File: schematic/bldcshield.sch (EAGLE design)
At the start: 51 parts, among them IC3 IR2101SMD, IC4 IR2101SMD, IC5 IR2101SMD, Q1 MOSFET-NCHANNELPTH2, Q2 MOSFET-NCHANNELPTH2, Q3 MOSFET-NCHANNELPTH2, Q4 MOSFET-NCHANNELPTH2, Q5 MOSFET-NCHANNELPTH2, Q6 MOSFET-NCHANNELPTH2, X1 MKDSN1,5/3-5,08, X2 MKDSN1,5/2-5,08

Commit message: redoing brf layout from scatch
deleted gerbers and backed up brd file
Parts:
- removed C20: 100pF, SmartPrj:C-EUC1206
- removed IC5: IR2101SMD, IR:IR2101SMD
- removed R29: 15k, SmartPrj:R-EU_R1206
- removed U$5: ARDUINO-NOHOLE, adafruit:ARDUINO-NOHOLE
- added C3: 100pF, SmartPrj:C-EUC1206
- added IC2: IR2101SMD, IR:IR2101SMD
- added Q7: MOSFET-NCHANNELPTH2, SparkFun:MOSFET-NCHANNELPTH2
- added R1: 200K, SmartPrj:R-EU_R1206
- Q3: value MOSFET-NCHANNELPTH2 -> Shield; device SparkFun:MOSFET-NCHANNELPTH2 -> adafruit:ARDUINOR3-NOIOREF-NOTEXT
- R10: value 10k -> 22k
- R11, R14, R6: value 10k -> 22
- R12, R13: value 22 -> 10k
- R15, R7: value 10k -> 100k
- R16, R8: value 22 -> 15k
- R17, R9: value 22 -> 22k
- R18: value 200K -> 22k
- R19: value 68k -> 22
- R2: value 22k -> 68k
- R20: value 100k -> 10k
- R21: value 15k -> 10k
- R22, R3: value 22k -> 22
- R23: value 22k -> 100k
- R24: value 100k -> 15k
- R25: value 15k -> 22k
- R27: value 22k -> 4.7k
- R28: value 100k -> 0.001; device SmartPrj:R-EU_R1206 -> resistor:R-US_R2512
- R4: value 4.7k -> 10k
- R5: value 0.001 -> 10k; device resistor:R-US_R2512 -> SmartPrj:R-EU_R1206
- X1: value MKDSN1,5/3-5,08 -> MKDSN1,5/2-5,08; device con-phoenix-508:MKDSN1,5/3-5,08 -> con-phoenix-508:MKDSN1,5/2-5,08
- X2: value MKDSN1,5/2-5,08 -> MKDSN1,5/3-5,08; device con-phoenix-508:MKDSN1,5/2-5,08 -> con-phoenix-508:MKDSN1,5/3-5,08
- renumbered C15 to C8, C16 to C5, C17 to C4, C18 to C1, C19 to C2, C21 to C7, D4 to D2, D5 to D1, IC4 to IC1
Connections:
- removed net N$20: C2.1, C20.1, C6.1, C7.1, IC1.COM, IC3.COM, IC5.COM, R10.1, R11.1, R14.1, R15.1, R19.1, R23.1, R27.1, R3.1, R5.1, R6.1, R7.1, X2-2.KL
- new net +3V3: Q3.3V
- net +5V: now also IC2.VCC, Q3.5V, Q3.VIN; no longer IC5.VCC, U$5.5V
- net BLDC1: now also C3.2, R7.2, R9.2, X2-1.KL; no longer C6.2, R2.2, R20.2, X1-1.KL
- net BLDC2: now also C6.2, IC2.VS, Q4.S, Q5.D, R15.2, R17.2, X2-2.KL; no longer C20.2, IC3.VS, Q3.S, Q4.D, R22.2, R24.2, X1-2.KL
- net BLDC3: now also IC3.VS, Q6.S, Q7.D, R23.2, R25.2, X2-3.KL; no longer IC5.VS, Q5.S, Q6.D, R26.2, R28.2, X1-3.KL
- net CURRENT: now also Q3.A0, Q5.S, Q7.S, R27.2, R28.2; no longer Q4.S, Q6.S, R4.2, R5.2, U$5.A0
- net EMF1: now also Q3.A3, R8.1; no longer R21.1, U$5.A3
- net EMF2: now also Q3.A2, R16.1; no longer R25.1, U$5.A2
- net EMF3: now also Q3.A1, R24.1; no longer R29.1, U$5.A1
- net GND: now also C2.1, C3.1, C6.1, C7.1, IC1.COM, IC2.COM, IC3.COM, Q3.GND, Q3.GND1, Q3.GND2, R10.1, R12.1, R13.1, R18.1, R2.1, R20.1, R21.1, R26.1, R28.1, R4.1, R5.1, X1-2.KL; no longer U$5.GND, U$5.GND1, U$5.GND2
- net HI_1: now also Q3.D12, R5.2; no longer R15.2, U$5.D12
- net HI_2: now also IC2.LIN, Q3.D10, R13.2; no longer IC3.LIN, R11.2, U$5.D10
- net HI_3: now also IC3.LIN, Q3.D8, R21.2; no longer IC5.LIN, R7.2, U$5.D8
- net LOW_VOLTAGE: now also Q3.A4/SDA, R1.1, R2.2; no longer R18.1, R19.2, U$5.A4
- net LO_1: now also Q3.D13, R4.2; no longer R14.2, U$5.D13
- net LO_2: now also IC2.HIN, Q3.D11, R12.2; no longer IC3.HIN, R10.2, U$5.D11
- net LO_3: now also IC3.HIN, Q3.D9, R20.2; no longer IC5.HIN, R6.2, U$5.D9
- net N$1: now also Q4.G, R11.1; no longer Q3.G, R13.1
- net N$10: now also R7.1, R8.2; no longer R20.1, R21.2
- net N$12: now also R17.1, R18.2; no longer R22.1, R23.2
- net N$13: now also IC3.HO, R19.2; no longer IC5.HO, R9.2
- net N$14: now also Q6.G, R19.1; no longer Q5.G, R9.1
- net N$15: now also Q7.G, R22.1; no longer Q6.G, R8.1
- net N$16: now also IC3.LO, R22.2; no longer IC5.LO, R8.2
- net N$17: now also IC3.VB; no longer IC5.VB
- net N$19: now also R15.1, R16.2; no longer R24.1, R25.2
- net N$2: now also R10.2, R9.1; no longer R2.1, R3.2
- net N$21: now also IC2.HO, R11.2; no longer IC3.HO, R13.2
- net N$23: now also Q5.G, R14.1; no longer Q4.G, R12.1
- net N$24: now also IC2.LO, R14.2; no longer IC3.LO, R12.2
- net N$25: now also IC2.VB; no longer IC3.VB
- net N$26: now also R25.1, R26.2; no longer R26.1, R27.2
- net N$28: now also R23.1, R24.2; no longer R28.1, R29.2
- net N$29: now also R3.2; no longer R17.2
- net N$30: now also R3.1; no longer R17.1
- net N$31: now also R6.1; no longer R16.1
- net N$32: now also R6.2; no longer R16.2
- net N$9: now also R27.1; no longer R4.1
- net VCC: now also Q3.AREF, Q4.D, Q6.D, R1.2, X1-1.KL; no longer Q3.D, Q5.D, R18.2, U$5.AREF, X2-1.KL
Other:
- moved on the sheet: C6, IC3, Q4, Q5, Q6, R10, R11, R12, R13, R14, R15, R16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

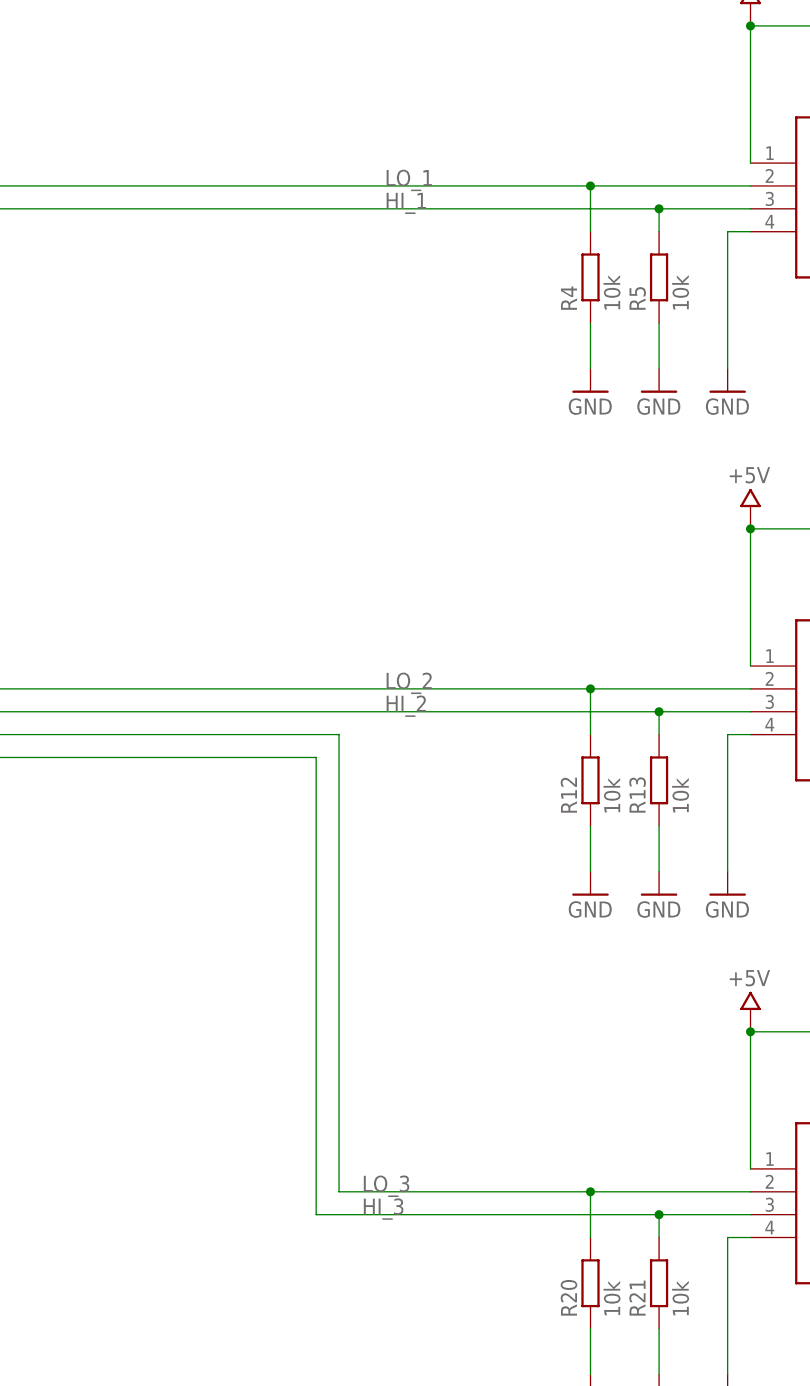
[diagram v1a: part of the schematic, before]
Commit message: Changed some labels on the sch
I think the finally routed pcb has never been committed.
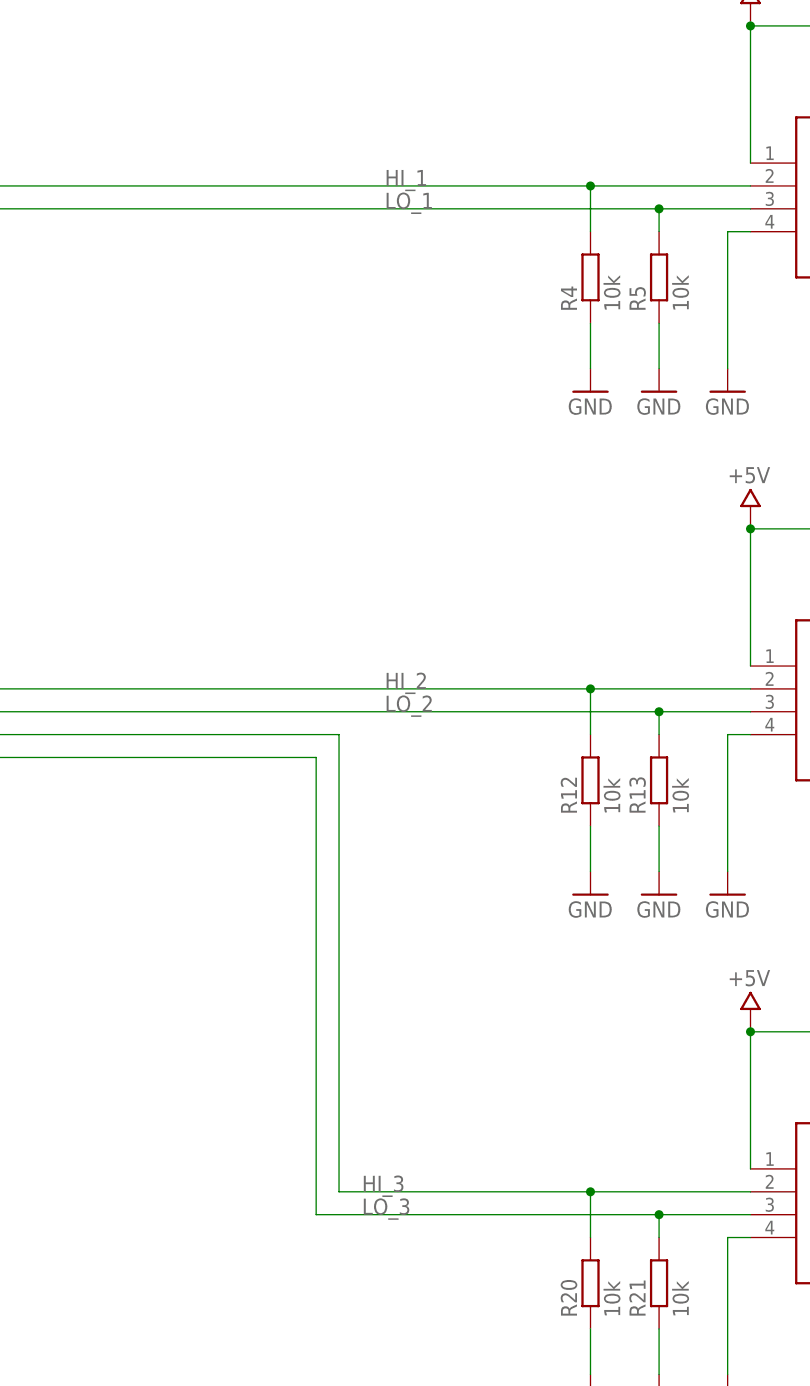
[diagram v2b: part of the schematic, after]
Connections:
- net HI_1: now also IC1.HIN, Q3.D13, R4.2; no longer IC1.LIN, Q3.D12, R5.2
- net HI_2: now also IC2.HIN, Q3.D11, R12.2; no longer IC2.LIN, Q3.D10, R13.2
- net HI_3: now also IC3.HIN, Q3.D9, R20.2; no longer IC3.LIN, Q3.D8, R21.2
- net LO_1: now also IC1.LIN, Q3.D12, R5.2; no longer IC1.HIN, Q3.D13, R4.2
- net LO_2: now also IC2.LIN, Q3.D10, R13.2; no longer IC2.HIN, Q3.D11, R12.2
- net LO_3: now also IC3.LIN, Q3.D8, R21.2; no longer IC3.HIN, Q3.D9, R20.2
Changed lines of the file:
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@@
 </segment>
 </net>
-<net name="LO_1" class="0">
+<net name="HI_1" class="0">
 <segment>
 <label x="-81.28" y="114.3" size="1.778" layer="95"/>
@@
 </segment>
 </net>
-<net name="HI_1" class="0">
+<net name="LO_1" class="0">
 <segment>
 <label x="-81.28" y="111.76" size="1.778" layer="95"/>
@@
 </segment>
 </net>
-<net name="LO_2" class="0">
+<net name="HI_2" class="0">
 <segment>
 <label x="-81.28" y="58.42" size="1.778" layer="95"/>
@@
 </segment>
 </net>
-<net name="HI_2" class="0">
+<net name="LO_2" class="0">
 <segment>
 <label x="-81.28" y="55.88" size="1.778" layer="95"/>
@@
 </segment>
 </net>
-<net name="LO_3" class="0">
+<net name="HI_3" class="0">
 <segment>
 <label x="-83.82" y="2.54" size="1.778" layer="95"/>
@@
 </segment>
 </net>
-<net name="HI_3" class="0">
+<net name="LO_3" class="0">
 <segment>
 <label x="-83.82" y="0" size="1.778" layer="95"/>

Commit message: working on arduino micro version schematic
also working on a hall effect code in the BLDC library
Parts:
- removed R12, R13, R20, R21, R4, R5: 10k, SmartPrj:R-EU_R1206
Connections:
- net GND: no longer R12.1, R13.1, R20.1, R21.1, R4.1, R5.1
- net HI_1: no longer R4.2
- net HI_2: no longer R12.2
- net HI_3: no longer R20.2
- net LO_1: no longer R5.2
- net LO_2: no longer R13.2
- net LO_3: no longer R21.2
- net VCC: no longer Q3.AREF
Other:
- moved on the sheet: C2, R1, R2, X1-1, X1-2

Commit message: updated schematic
updated schematic: removed pull down resistors and added 12V regulator
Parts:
- added C24: 1uF, SmartPrj:C-EUC1206
- added C25: 0.1u, SmartPrj:C-EUC1206
- added R32: 240, SmartPrj:R-EU_R1206
- added R33: 2.2k, SmartPrj:R-EU_R1206
- added U3: LM317DCY, Texas Instruments_By_element14_Batch_1:LM317DCY
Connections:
- new net +12V: C24.2, D1.A, D2.A, D3.A, IC1.VCC, IC2.VCC, IC3.VCC, R32.1, U3.OUTPUT, U3.OUTPUT_2
- new net N$5: R32.2, R33.1, U3.ADJUST
- net +5V: no longer D1.A, D2.A, D3.A, IC1.VCC, IC2.VCC, IC3.VCC
- net GND: now also C24.1, C25.1, R33.2
- net VCC: now also C25.2, U3.INPUT
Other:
- note added: "+12V REG"
- moved on the sheet: C2, R1, R2, X1-1, X1-2

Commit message: updated schematic and code
added hall effect sensors
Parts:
- removed C3, C6, C7: 100pF, SmartPrj:C-EUC1206
- removed R10, R17, R18, R25, R26, R9: 22k, SmartPrj:R-EU_R1206
- removed R15, R23: 100k, SmartPrj:R-EU_R1206
- removed R16, R24, R8: 15k, SmartPrj:R-EU_R1206
- added JP1: (no value), SparkFun-Connectors:PINHD-2X3
- added R4, R5: 10k, SmartPrj:R-EU_R1206
- R7: value 100k -> 10k
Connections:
- removed net EMF1: Q3.A3, R8.1
- removed net EMF2: Q3.A2, R16.1
- removed net EMF3: Q3.A1, R24.1
- removed net N$12: R17.1, R18.2
- removed net N$19: R15.1, R16.2
- removed net N$2: R10.2, R9.1
- removed net N$26: R25.1, R26.2
- removed net N$28: R23.1, R24.2
- new net N$4: JP1.2, Q3.A0, R7.1
- new net N$7: JP1.6, Q3.A2, R4.1
- net +5V: now also JP1.1, R4.2, R5.2, R7.2
- net BLDC1: no longer C3.2, R7.2, R9.2
- net BLDC2: no longer C6.2, R15.2, R17.2
- net BLDC3: no longer C7.2, R23.2, R25.2
- net CURRENT: now also Q3.A3; no longer Q3.A0
- net GND: now also JP1.5; no longer C3.1, C6.1, C7.1, R10.1, R18.1, R26.1
- net N$10: now also JP1.4, Q3.A1, R5.1; no longer R7.1, R8.2
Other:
- moved on the sheet: R7

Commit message: continuing to work on pcb
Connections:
- net N$4: now also Q3.A2; no longer Q3.A0
- net N$7: now also Q3.A0; no longer Q3.A2
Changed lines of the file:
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@@
 <net name="N$7" class="3">
 <segment>
-<pinref part="Q3" gate="G$1" pin="A2"/>
-<wire x1="-248.92" y1="83.82" x2="-236.22" y2="83.82" width="0.1524" layer="91"/>
-<wire x1="-248.92" y1="83.82" x2="-254" y2="88.9" width="0.1524" layer="91"/>
 <pinref part="JP1" gate="A" pin="6"/>
 <wire x1="-287.02" y1="88.9" x2="-264.16" y2="88.9" width="0.1524" layer="91"/>
 <pinref part="R4" gate="G$1" pin="1"/>
 <wire x1="-264.16" y1="88.9" x2="-264.16" y2="96.52" width="0.1524" layer="91"/>
-<wire x1="-254" y1="88.9" x2="-264.16" y2="88.9" width="0.1524" layer="91"/>
 <junction x="-264.16" y="88.9"/>
+<pinref part="Q3" gate="G$1" pin="A0"/>
+<wire x1="-264.16" y1="88.9" x2="-236.22" y2="88.9" width="0.1524" layer="91"/>
 </segment>
 </net>
@@
 <wire x1="-287.02" y1="93.98" x2="-274.32" y2="93.98" width="0.1524" layer="91"/>
 <wire x1="-274.32" y1="93.98" x2="-254" y2="93.98" width="0.1524" layer="91"/>
-<pinref part="Q3" gate="G$1" pin="A0"/>
-<wire x1="-248.92" y1="88.9" x2="-236.22" y2="88.9" width="0.1524" layer="91"/>
-<wire x1="-254" y1="93.98" x2="-248.92" y2="88.9" width="0.1524" layer="91"/>
 <junction x="-274.32" y="93.98"/>
+<wire x1="-254" y1="93.98" x2="-243.84" y2="83.82" width="0.1524" layer="91"/>
+<pinref part="Q3" gate="G$1" pin="A2"/>
+<wire x1="-243.84" y1="83.82" x2="-236.22" y2="83.82" width="0.1524" layer="91"/>
 </segment>
 </net>
